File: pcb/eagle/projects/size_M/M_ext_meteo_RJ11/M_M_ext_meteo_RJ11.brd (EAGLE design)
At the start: 10 parts, among them J1 RJ11

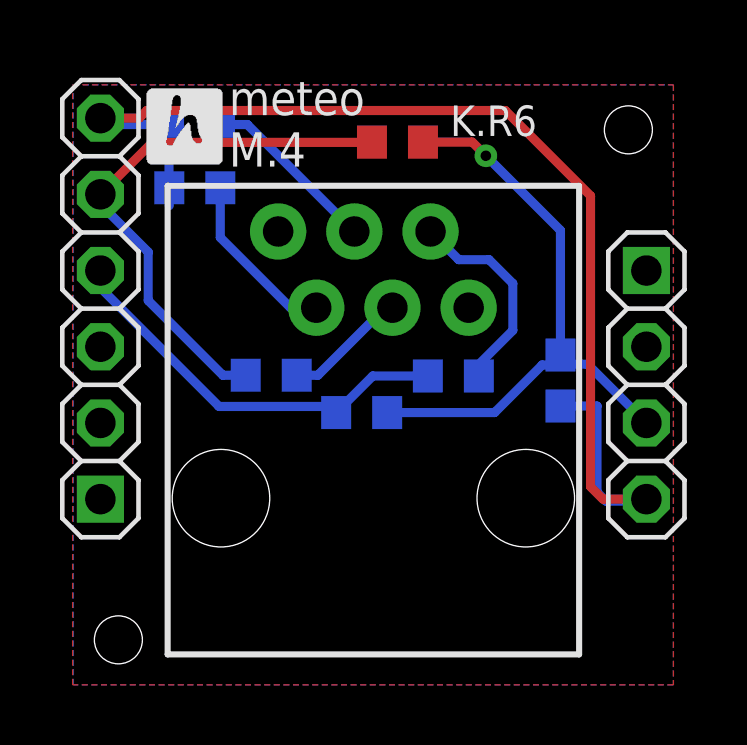
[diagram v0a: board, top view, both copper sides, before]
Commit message: changed values of used resistors
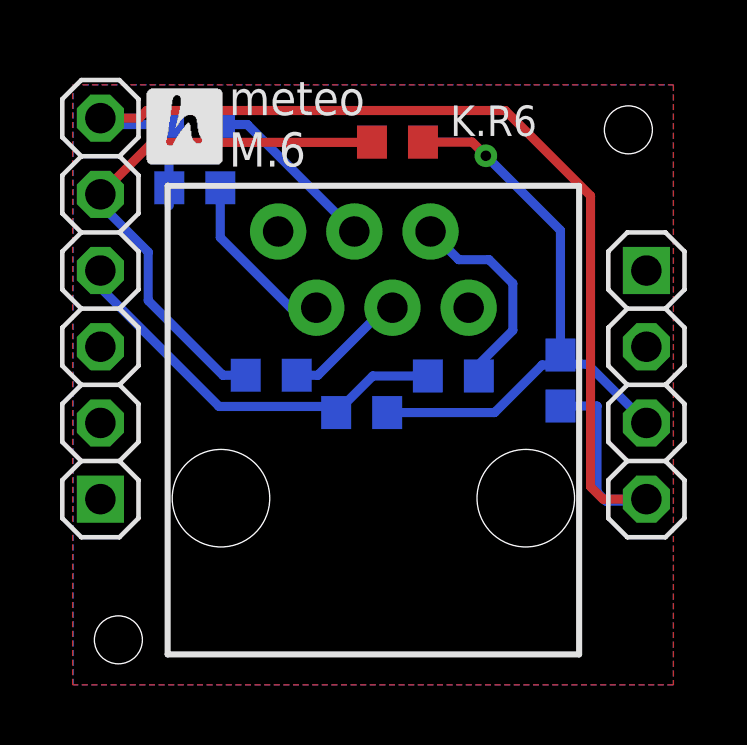
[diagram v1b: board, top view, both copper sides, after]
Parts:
- K.R1, K.R3, K.R4, K.R5: value 1k -> 100
- K.R2, K.R6: value 4k7 -> 10k
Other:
- board text added: "meteo M.6"
- board text removed: "meteo M.4"
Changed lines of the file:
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@@
 <circle x="2" y="2" radius="1.9" width="0.1" layer="52"/>
 <text x="5.6854" y="17.775" size="1.143" layer="21">meteo
-M.4</text>
+M.6</text>
 <rectangle x1="3.0607" y1="17.8435" x2="5.3721" y2="17.8689" layer="21"/>
 <rectangle x1="3.0099" y1="17.8689" x2="5.3975" y2="17.8943" layer="21"/>
@@
 <attribute name="SPICEPREFIX" value="C" x="16.7358" y="10.6426" size="1.778" layer="28" rot="MR270" display="off"/>
 </element>
-<element name="K.R3" library="rcl" library_urn="urn:adsk.eagle:library:334" package="R0603" package3d_urn="urn:adsk.eagle:package:23555/3" value="1k" x="7.0952" y="10.8204" smashed="yes" rot="MR180">
+<element name="K.R3" library="rcl" library_urn="urn:adsk.eagle:library:334" package="R0603" package3d_urn="urn:adsk.eagle:package:23555/3" value="100" x="7.0952" y="10.8204" smashed="yes" rot="MR180">
 <attribute name="NAME" x="4.4536" y="10.0584" size="1.016" layer="26" rot="MR180"/>
 <attribute name="POPULARITY" value="70" x="7.0952" y="10.8204" size="1.778" layer="28" rot="MR180" display="off"/>
@@
 <attribute name="VALUE" x="6.4602" y="12.7254" size="1.27" layer="28" rot="MR180"/>
 </element>
-<element name="K.R4" library="rcl" library_urn="urn:adsk.eagle:library:334" package="R0603" package3d_urn="urn:adsk.eagle:package:23555/3" value="1k" x="13.1658" y="10.795" smashed="yes" rot="MR180">
+<element name="K.R4" library="rcl" library_urn="urn:adsk.eagle:library:334" package="R0603" package3d_urn="urn:adsk.eagle:package:23555/3" value="100" x="13.1658" y="10.795" smashed="yes" rot="MR180">
 <attribute name="NAME" x="12.353" y="9.9822" size="1.016" layer="26" rot="MR180"/>
 <attribute name="POPULARITY" value="70" x="13.1658" y="10.795" size="1.778" layer="28" rot="MR180" display="off"/>
@@
 <attribute name="VALUE" x="12.5308" y="12.7" size="1.27" layer="28" rot="MR180"/>
 </element>
-<element name="K.R5" library="rcl" library_urn="urn:adsk.eagle:library:334" package="R0603" package3d_urn="urn:adsk.eagle:package:23555/3" value="1k" x="4.538" y="19.177" smashed="yes" rot="MR180">
+<element name="K.R5" library="rcl" library_urn="urn:adsk.eagle:library:334" package="R0603" package3d_urn="urn:adsk.eagle:package:23555/3" value="100" x="4.538" y="19.177" smashed="yes" rot="MR180">
 <attribute name="NAME" x="6.2144" y="19.558" size="1.016" layer="26" rot="MR180"/>
 <attribute name="POPULARITY" value="70" x="4.538" y="19.177" size="1.778" layer="28" rot="MR180" display="off"/>
@@
 <attribute name="VALUE" x="8.849" y="3.9276" size="0.6096" layer="27" font="vector" ratio="20"/>
 </element>
-<element name="K.R1" library="rcl" library_urn="urn:adsk.eagle:library:334" package="R0603" package3d_urn="urn:adsk.eagle:package:23555/3" value="1k" x="4.5466" y="17.0688" smashed="yes" rot="MR180">
+<element name="K.R1" library="rcl" library_urn="urn:adsk.eagle:library:334" package="R0603" package3d_urn="urn:adsk.eagle:package:23555/3" value="100" x="4.5466" y="17.0688" smashed="yes" rot="MR180">
 <attribute name="NAME" x="2.6416" y="16.1798" size="1.016" layer="26" rot="MR180"/>
 <attribute name="POPULARITY" value="70" x="4.5466" y="17.0688" size="1.778" layer="28" rot="MR180" display="off"/>
 <attribute name="SPICEPREFIX" value="R" x="4.5466" y="17.0688" size="1.778" layer="28" rot="MR180" display="off"/>
 </element>
-<element name="K.R2" library="rcl" library_urn="urn:adsk.eagle:library:334" package="R0603" package3d_urn="urn:adsk.eagle:package:23555/3" value="4k7" x="10.1092" y="9.5758" smashed="yes" rot="MR0">
+<element name="K.R2" library="rcl" library_urn="urn:adsk.eagle:library:334" package="R0603" package3d_urn="urn:adsk.eagle:package:23555/3" value="10k" x="10.1092" y="9.5758" smashed="yes" rot="MR0">
 <attribute name="NAME" x="11.5824" y="7.7978" size="1.016" layer="26" rot="MR0"/>
 <attribute name="POPULARITY" value="70" x="10.1092" y="9.5758" size="1.778" layer="28" rot="MR0" display="off"/>
 <attribute name="SPICEPREFIX" value="R" x="10.1092" y="9.5758" size="1.778" layer="28" rot="MR0" display="off"/>
 </element>
-<element name="K.R6" library="rcl" library_urn="urn:adsk.eagle:library:334" package="R0603" package3d_urn="urn:adsk.eagle:package:23555/3" value="4k7" x="11.303" y="18.5928" smashed="yes" rot="R180">
+<element name="K.R6" library="rcl" library_urn="urn:adsk.eagle:library:334" package="R0603" package3d_urn="urn:adsk.eagle:package:23555/3" value="10k" x="11.303" y="18.5928" smashed="yes" rot="R180">
 <attribute name="NAME" x="15.9512" y="19.812" size="1.016" layer="25" rot="R180"/>
 <attribute name="POPULARITY" value="70" x="11.303" y="18.5928" size="1.778" layer="27" rot="R180" display="off"/>

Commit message: bugfix: swapped GPIOs to be handled interrups during slepp
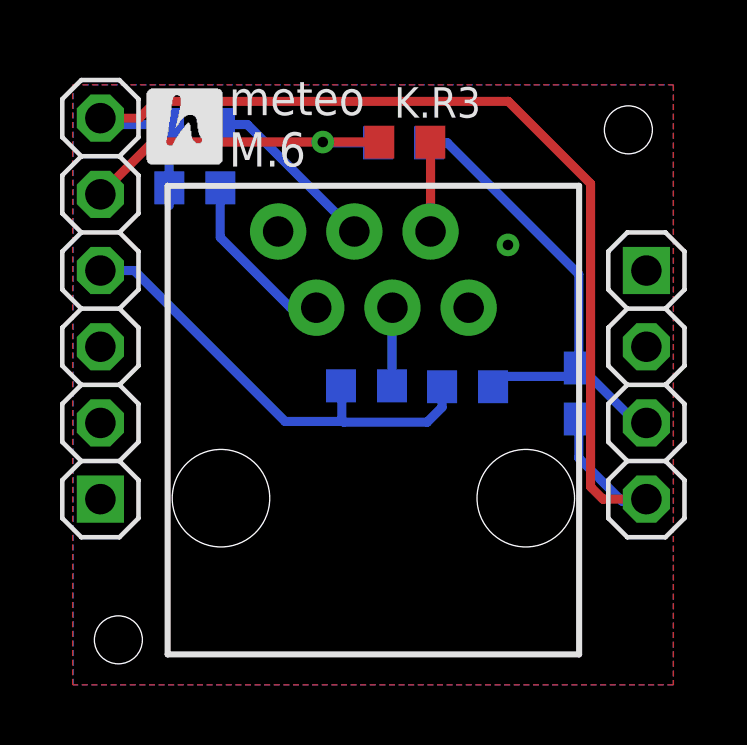
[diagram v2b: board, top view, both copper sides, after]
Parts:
- moved K.R3 8.96 mm to (11.5, 18.6), flipped to the top, turned to 0 degrees
- moved K.R2 3.63 mm to (13.6, 10.4)
- moved K.R4 2.91 mm to (10.3, 10.5)
- moved K.C1 0.75 mm to (17.3, 10.2)
- moved K.R6 0.20 mm to (11.5, 18.6), flipped to the bottom, turned to 0 degrees
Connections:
- removed net N$6: J1.4, K.R3.2
- new net N$4: J1.4, K.R4.2
- net N$1: now also K.R3.2; no longer K.R4.2
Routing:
- net N$2: track 18.3 -> 11.9 mm, vias 0 -> 1
- net VCC: track 20.3 -> 16.1 mm, vias 1 -> 0
- net N$6: track 4.12 -> 0.00 mm
- net N$1: track 7.01 -> 2.98 mm
- net N$4: track 0.00 -> 2.61 mm
- net N$3: track 13.7 -> 15.9 mm
- net GND: track 40.3 -> 39.1 mm, vias 0 -> 1

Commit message: PCB v7 * 14 pin attiny is main adapter chip now. * changed adapter pin meaning (a1-a5, swapped RX-TX, VUSB replaced by A5, top most pin changed from GND to A4) * changed usb chip of main board
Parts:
- moved K.R6 1.27 mm to (12.8, 18.5)
- moved K.R1 1.22 mm to (3.73, 16.2), turned to 270 degrees
- moved K.R4 1.14 mm to (11.4, 10.6), turned to 0 degrees
- moved K.R2 0.98 mm to (14.6, 10.6)
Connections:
- net GND: no longer JP2.6
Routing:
- net GND: track 39.1 -> 6.38 mm
- net VCC: track 16.1 -> 14.6 mm
- net N$3: track 15.9 -> 15.0 mm
- net N$2: track 11.9 -> 12.7 mm
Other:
- board text added: "meteo M.7"
- board text removed: "meteo M.6"

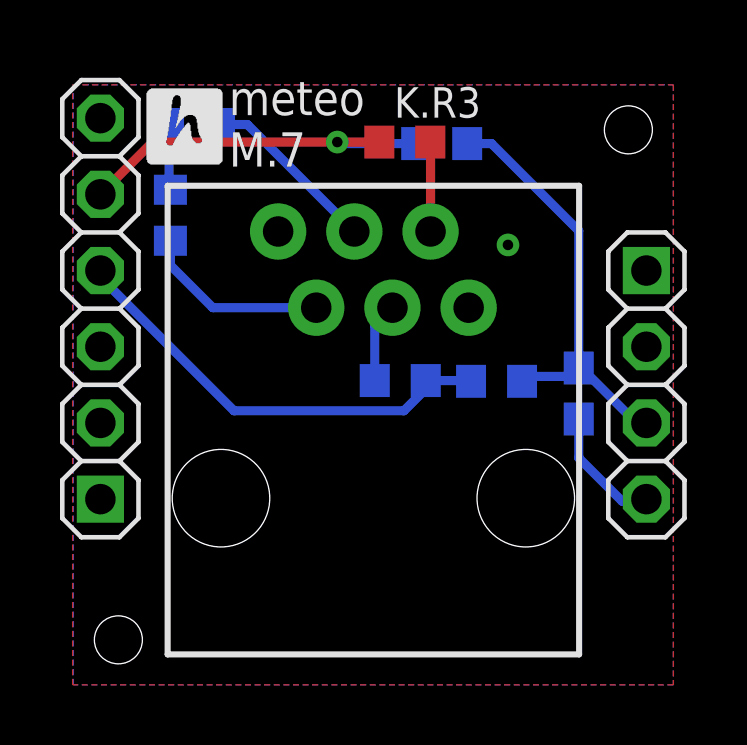
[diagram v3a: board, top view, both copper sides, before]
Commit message: version 8 main changes * ideal diode separated 3v3 DC-DC to protect it from back current * smaller package of ina 219 * usage of tssop attiny v2 in adapter * and change of PA5 to PB2 with ^ and ~ (originally used for shield power switch - now PB3) * step motor shield * out signal for BT module
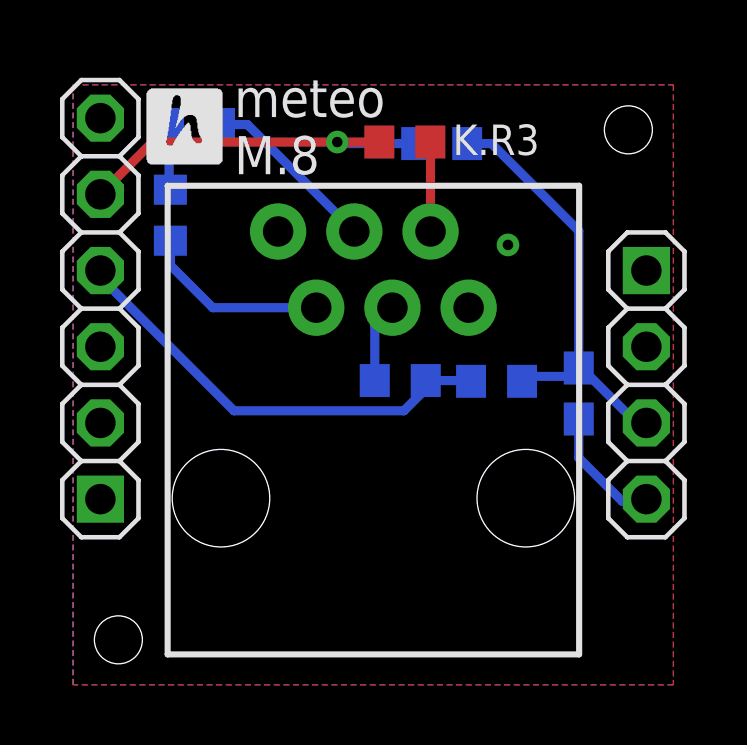
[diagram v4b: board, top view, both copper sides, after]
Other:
- board text added: "meteo M.8"
- board text removed: "meteo M.7"
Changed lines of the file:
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@@
 <grid distance="1" unitdist="mil" unit="mm" style="lines" multiple="1" display="no" altdistance="5" altunitdist="mil" altunit="mil"/>
 <layers>
-<layer number="1" name="Top" color="4" fill="1" visible="yes" active="yes"/>
-<layer number="16" name="Bottom" color="1" fill="1" visible="yes" active="yes"/>
+<layer number="1" name="Top" color="4" fill="1" visible="no" active="yes"/>
+<layer number="16" name="Bottom" color="1" fill="1" visible="no" active="yes"/>
 <layer number="17" name="Pads" color="2" fill="1" visible="yes" active="yes"/>
 <layer number="18" name="Vias" color="2" fill="1" visible="yes" active="yes"/>
-<layer number="19" name="Unrouted" color="6" fill="1" visible="yes" active="yes"/>
-<layer number="20" name="Dimension" color="24" fill="1" visible="yes" active="yes"/>
+<layer number="19" name="Unrouted" color="6" fill="1" visible="no" active="yes"/>
+<layer number="20" name="Dimension" color="24" fill="1" visible="no" active="yes"/>
 <layer number="21" name="tPlace" color="7" fill="1" visible="yes" active="yes"/>
-<layer number="22" name="bPlace" color="7" fill="1" visible="yes" active="yes"/>
+<layer number="22" name="bPlace" color="7" fill="1" visible="no" active="yes"/>
 <layer number="23" name="tOrigins" color="15" fill="1" visible="yes" active="yes"/>
-<layer number="24" name="bOrigins" color="15" fill="1" visible="yes" active="yes"/>
+<layer number="24" name="bOrigins" color="15" fill="1" visible="no" active="yes"/>
 <layer number="25" name="tNames" color="7" fill="1" visible="yes" active="yes"/>
-<layer number="26" name="bNames" color="7" fill="1" visible="yes" active="yes"/>
+<layer number="26" name="bNames" color="7" fill="1" visible="no" active="yes"/>
 <layer number="27" name="tValues" color="7" fill="1" visible="no" active="yes"/>
 <layer number="28" name="bValues" color="7" fill="1" visible="no" active="yes"/>
-<layer number="29" name="tStop" color="7" fill="3" visible="no" active="yes"/>
+<layer number="29" name="tStop" color="7" fill="3" visible="yes" active="yes"/>
 <layer number="30" name="bStop" color="7" fill="6" visible="no" active="yes"/>
 <layer number="31" name="tCream" color="7" fill="4" visible="no" active="yes"/>
@@
 <layer number="37" name="tTest" color="7" fill="1" visible="no" active="yes"/>
 <layer number="38" name="bTest" color="7" fill="1" visible="no" active="yes"/>
-<layer number="39" name="tKeepout" color="4" fill="11" visible="yes" active="yes"/>
-<layer number="40" name="bKeepout" color="1" fill="11" visible="yes" active="yes"/>
-<layer number="41" name="tRestrict" color="4" fill="10" visible="yes" active="yes"/>
-<layer number="42" name="bRestrict" color="1" fill="10" visible="yes" active="yes"/>
+<layer number="39" name="tKeepout" color="4" fill="11" visible="no" active="yes"/>
+<layer number="40" name="bKeepout" color="1" fill="11" visible="no" active="yes"/>
+<layer number="41" name="tRestrict" color="4" fill="10" visible="no" active="yes"/>
+<layer number="42" name="bRestrict" color="1" fill="10" visible="no" active="yes"/>
 <layer number="43" name="vRestrict" color="2" fill="10" visible="no" active="yes"/>
 <layer number="44" name="Drills" color="7" fill="1" visible="no" active="yes"/>
@@
 <layer number="46" name="Milling" color="3" fill="1" visible="no" active="yes"/>
 <layer number="47" name="Measures" color="7" fill="1" visible="no" active="yes"/>
-<layer number="48" name="Document" color="7" fill="1" visible="no" active="yes"/>
+<layer number="48" name="Document" color="7" fill="1" visible="yes" active="yes"/>
 <layer number="49" name="Reference" color="7" fill="1" visible="no" active="yes"/>
 <layer number="50" name="dxf" color="7" fill="1" visible="no" active="no"/>
-<layer number="51" name="tDocu" color="7" fill="1" visible="yes" active="yes"/>
-<layer number="52" name="bDocu" color="7" fill="1" visible="yes" active="yes"/>
+<layer number="51" name="tDocu" color="7" fill="1" visible="no" active="yes"/>
+<layer number="52" name="bDocu" color="7" fill="1" visible="no" active="yes"/>
 <layer number="53" name="tGND_GNDA" color="7" fill="9" visible="no" active="no"/>
 <layer number="54" name="bGND_GNDA" color="1" fill="9" visible="no" active="no"/>
@@
 <hole x="2" y="2" drill="1.6"/>
 <circle x="2" y="2" radius="1.9" width="0.1" layer="52"/>
-<text x="5.6854" y="17.775" size="1.143" layer="21">meteo
-M.7</text>
+<text x="5.8632" y="17.521" size="1.27" layer="21">meteo
+M.8</text>
 <rectangle x1="3.0607" y1="17.8435" x2="5.3721" y2="17.8689" layer="21"/>
 <rectangle x1="3.0099" y1="17.8689" x2="5.3975" y2="17.8943" layer="21"/>
@@
 </element>
 <element name="K.R3" library="rcl" library_urn="urn:adsk.eagle:library:334" package="R0603" package3d_urn="urn:adsk.eagle:package:23555/3" value="100" x="11.5484" y="18.5928" smashed="yes">
-<attribute name="NAME" x="11.1928" y="19.4056" size="1.016" layer="25"/>
+<attribute name="NAME" x="13.1486" y="18.161" size="1.016" layer="25"/>
 <attribute name="POPULARITY" value="70" x="11.5484" y="18.5928" size="1.778" layer="27" display="off"/>
 <attribute name="SPICEPREFIX" value="R" x="11.5484" y="18.5928" size="1.778" layer="27" display="off"/>
